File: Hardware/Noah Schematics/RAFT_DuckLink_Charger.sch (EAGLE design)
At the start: 27 parts, among them Q1_Q2 SI7288DP-T1-GE3, Q3 2N7002, U1 BQ24650RVAR

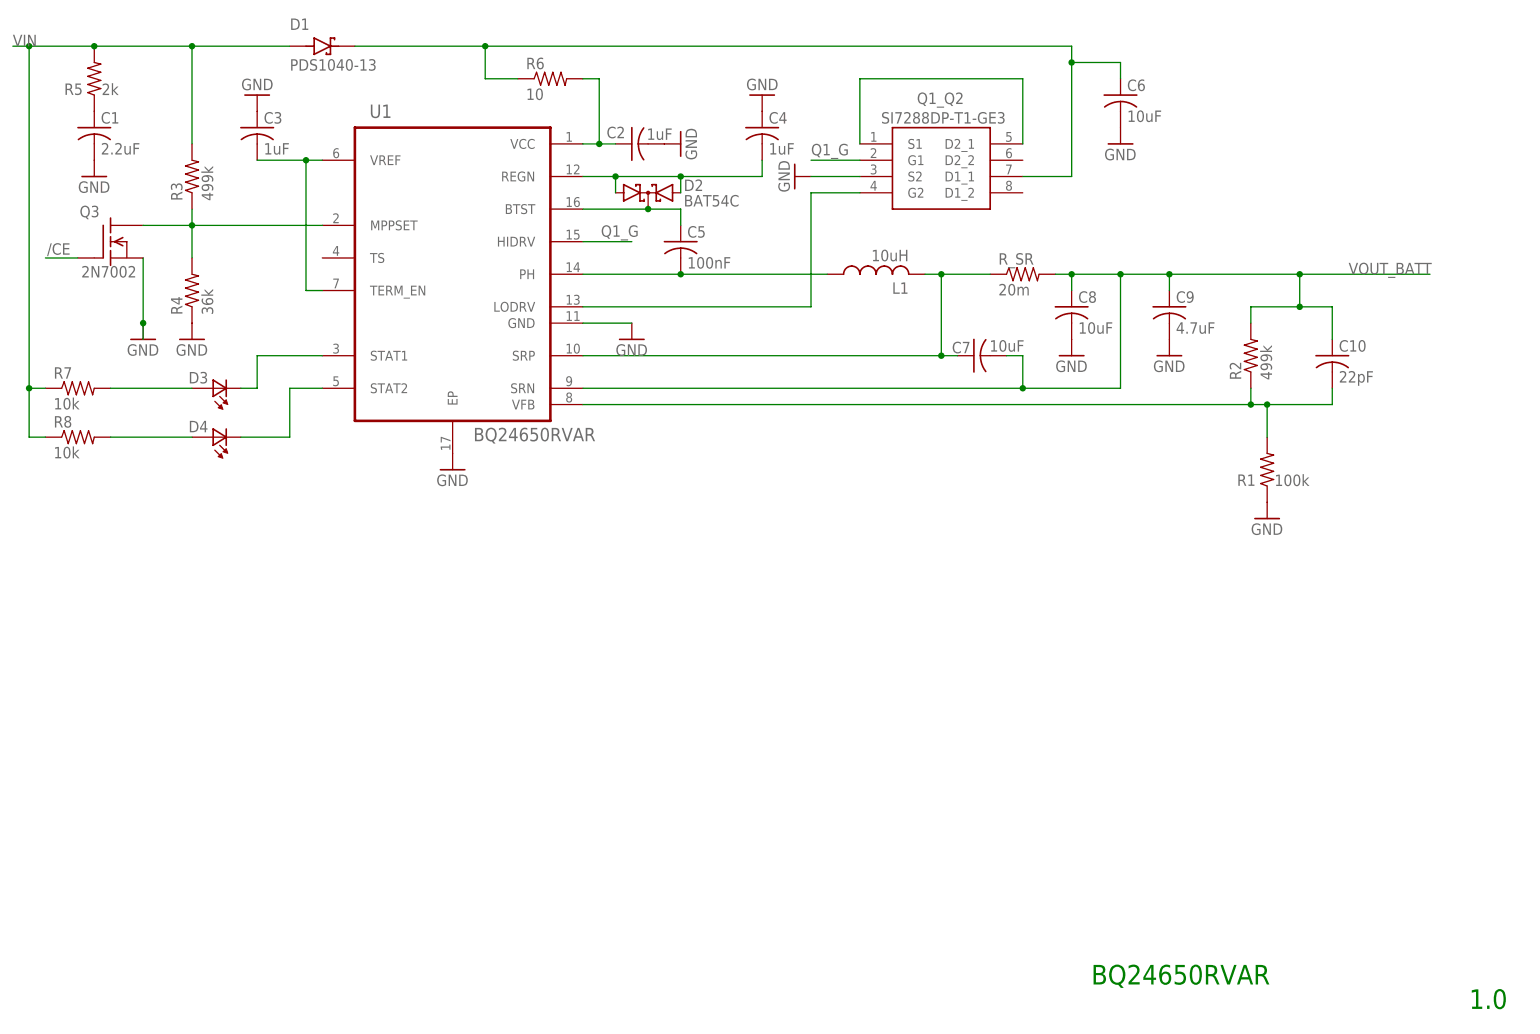
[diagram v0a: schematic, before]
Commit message: Added updated Charger with specified components
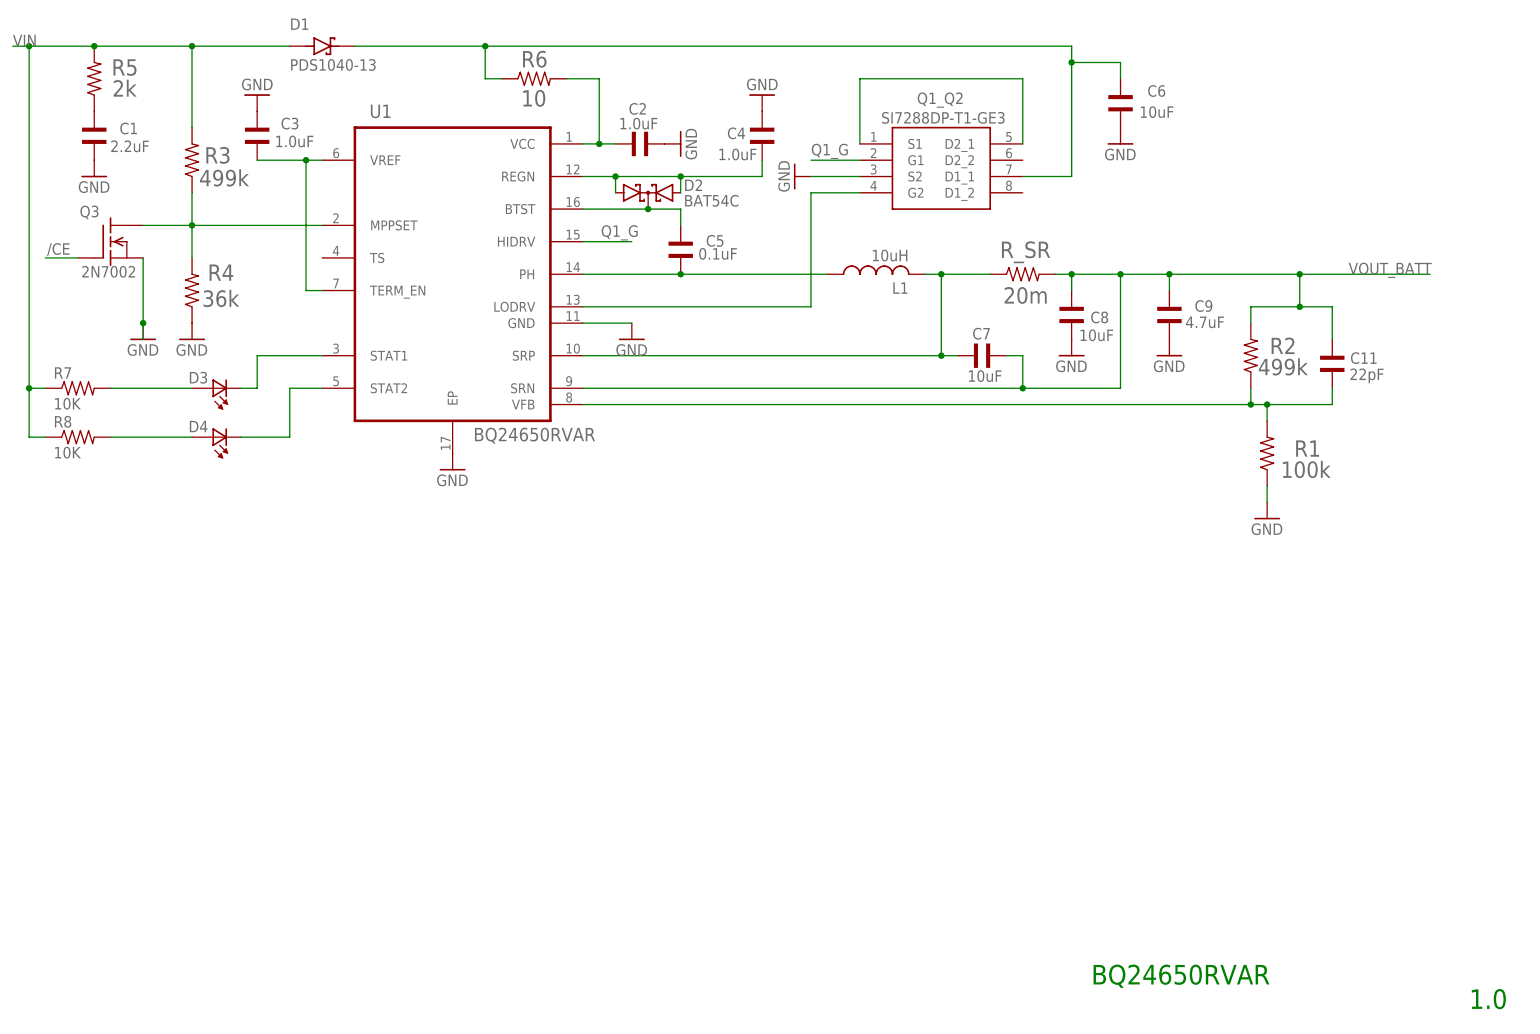
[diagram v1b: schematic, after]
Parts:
- removed C10: 22pF, resistor:C-USC0402
- added C11: 22pF, GCM1555C1H220JA16J:GCM1555C1H220JA16J
- C1: device resistor:C-USC0402 -> GRM155D80J225ME95D:GRM155D80J225ME95D
- C2, C3, C4: value 1uF -> 1.0uF; device resistor:C-USC0402 -> GCM155C71A105KE38D:GCM155C71A105KE38D
- C5: value 100nF -> 0.1uF; device resistor:C-USC0402 -> GRM155R71C104KA88D:GRM155R71C104KA88D
- C6, C7, C8: device resistor:C-USC0402 -> GRM155C80J106ME11D:GRM155C80J106ME11D
- C9: device resistor:C-USC0402 -> GRM155R60J475ME87D:GRM155R60J475ME87D
- R1: device resistor:R-US_R0402 -> CRCW0402100KFKED:CRCW0402100KFKED
- R2, R3: device resistor:R-US_R0402 -> CRCW0402499KFKED:CRCW0402499KFKED
- R4: device resistor:R-US_R0402 -> CRCW040236K0FKED:CRCW040236K0FKED
- R5: device resistor:R-US_R0402 -> CRCW04022K00FKED:CRCW04022K00FKED
- R6: device resistor:R-US_R0402 -> CRCW040210R0JNEDC:CRCW040210R0JNEDC
- R7, R8: value 10k -> 10K; device resistor:R-US_R0402 -> CRCW040210K0JNED:CRCW040210K0JNED
- R_SR: device resistor:R-US_R0402 -> ERJ-3BWFR020V:ERJ-3BWFR020V
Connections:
- net GND: now also C1.1, C3.2, C4.2, C6.1, C8.1, C9.1; no longer C1.2, C3.1, C4.1, C6.2, C8.2, C9.2
- net N$2: now also C3.1; no longer C3.2
- net N$3: now also C1.2; no longer C1.1
- net N$5: now also C4.1; no longer C4.2
- net N$6: now also C5.1; no longer C5.2
- net N$7: now also C5.2; no longer C5.1
- net N$9: now also C11.1; no longer C10.2
- net SC_VIN: now also C6.2; no longer C6.1
- net VOUT_BATT: now also C11.2, C8.2, C9.2; no longer C10.1, C8.1, C9.1
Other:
- moved on the sheet: R1, R3, R6
